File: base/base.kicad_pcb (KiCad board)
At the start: 2 copper layers, 100 x 100 mm, 32 parts, among them J1 FTDI, J2 Barrel_Jack, J3 CONN_01X40, SW1 RESET, SW2 POWER, U1 Z80CPU, U2 27C256, U3 7404, U4 55257, U5 7432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

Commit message: Added power indicator light and changed FTDI footprint
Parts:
- added D2: LED, LEDs:LED_D3.0mm, F.Cu at (105.4, 154.9)
- added R4: 470, Resistors_THT:R_Axial_DIN0207_L6.3mm_D2.5mm_P7.62mm_Horizontal, F.Cu at (115.6, 154.9)
- J1: footprint Pin_Headers:Pin_Header_Straight_1x06_Pitch2.54mm -> Pin_Headers:Pin_Header_Angled_1x06_Pitch2.54mm
- moved J1 7.62 mm to (133.3, 71.9)
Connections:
- J1 pad 2: CTS -> (no net)
- J1 pad 3: Net-(J1-Pad3) -> (no net)
- J1 pad 6: RTS -> (no net)
- SW2 pad 1: Net-(SW2-Pad1) -> (no net)
- SW2 pad 2: Net-(SW2-Pad2) -> (no net)
- U2 pad 1: Net-(U2-Pad1) -> (no net)
- U5 pad 10: Net-(U5-Pad10) -> (no net)
- U5 pad 8: Net-(U5-Pad8) -> (no net)
- U5 pad 9: Net-(U5-Pad9) -> (no net)
- U6 pad 17: Net-(U6-Pad17) -> (no net)
- U6 pad 23: Net-(U6-Pad23) -> (no net)
- U6 pad 24: Net-(U6-Pad24) -> (no net)
- U6 pad 29: Net-(U6-Pad29) -> (no net)
- U6 pad 31: Net-(U6-Pad31) -> (no net)
- U6 pad 32: Net-(U6-Pad32) -> (no net)
- U6 pad 33: Net-(U6-Pad33) -> (no net)
- U6 pad 34: Net-(U6-Pad34) -> (no net)
- U6 pad 36: Net-(U6-Pad36) -> (no net)
- U6 pad 37: Net-(U6-Pad37) -> (no net)
- U6 pad 38: Net-(U6-Pad38) -> (no net)
- U6 pad 39: Net-(U6-Pad39) -> (no net)
- X1 pad 1: Net-(X1-Pad1) -> (no net)
- X2 pad 1: Net-(X2-Pad1) -> (no net)
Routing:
- net RX: track 57.0 -> 49.3 mm
- net +5V: track 394.2 -> 400.7 mm
- net TX: track 65.7 -> 59.4 mm
- net Net-(D2-Pad1): track 0.00 -> 2.54 mm
- net (no net): track 0.00 -> 1.27 mm
- net Net-(J1-Pad3): track 0.79 -> 0.00 mm
- net Net-(U5-Pad8): track 0.63 -> 0.00 mm
- net Net-(U5-Pad10): track 0.63 -> 0.00 mm
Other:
- board text added: "CTS"
- board text added: "RTS"
- board text added: "RX<"
- board text added: "TX>"
- board text added: "Vcc"

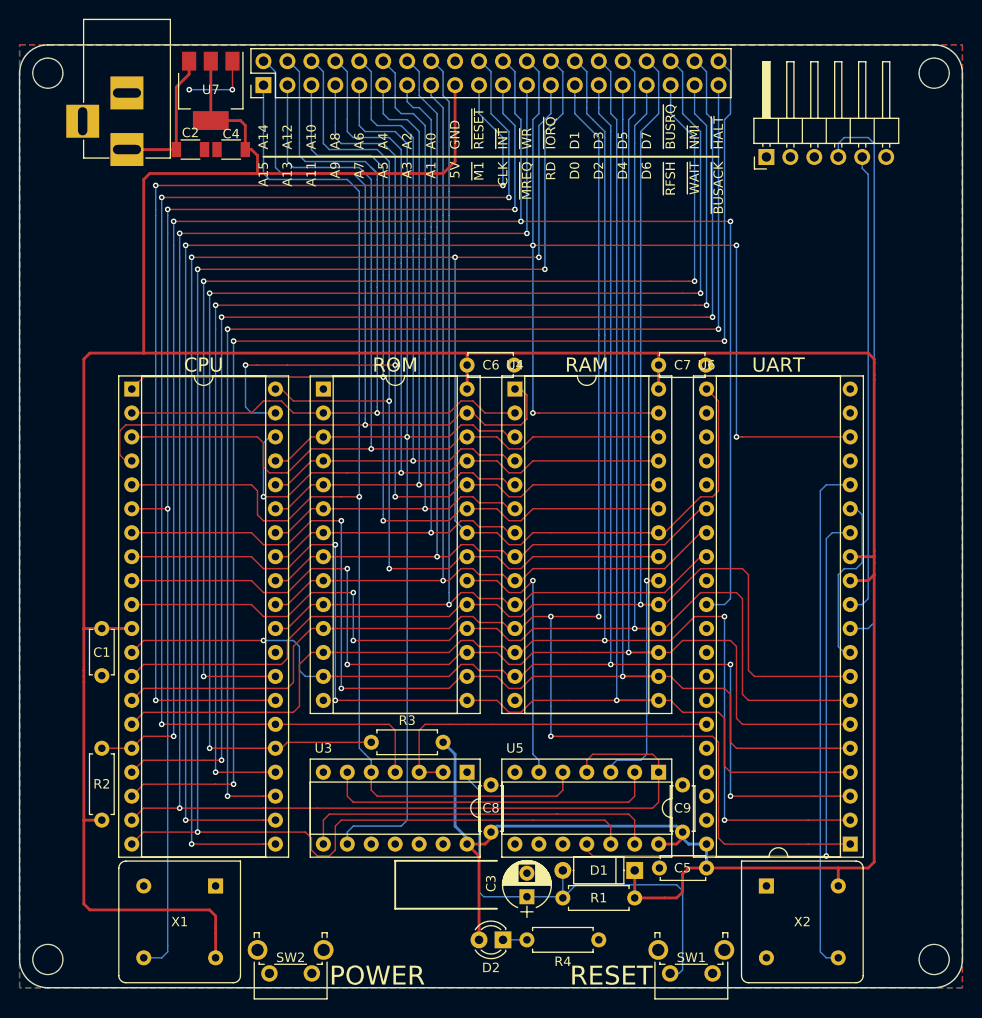
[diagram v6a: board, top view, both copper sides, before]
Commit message: Added soft power button
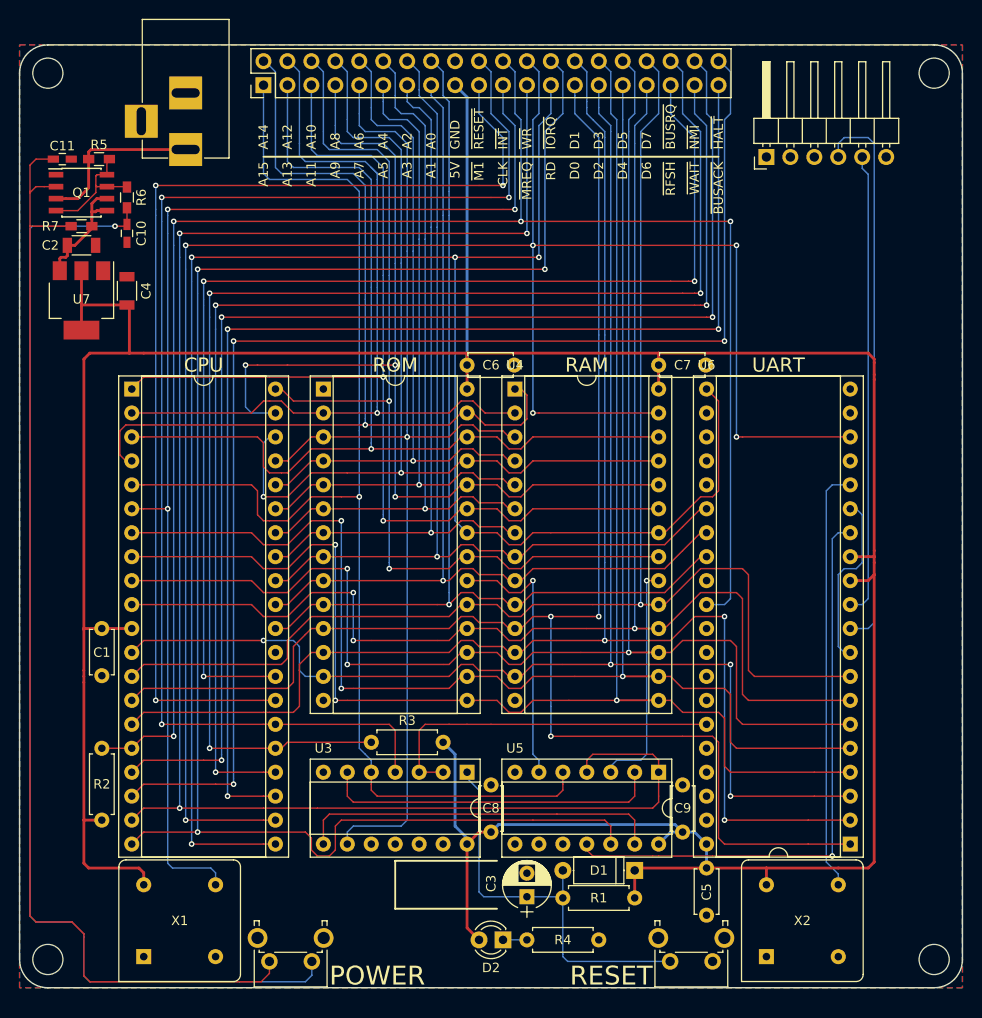
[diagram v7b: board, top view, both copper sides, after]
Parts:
- added C10: 1 uF, Capacitors_SMD:C_0603_HandSoldering, F.Cu at (65.5, 80.0)
- added C11: .1 uF, Capacitors_SMD:C_0603_HandSoldering, F.Cu at (58.7, 72.1)
- added Q1: IRF7309IPBF, Housings_SOIC:SOIC-8_3.9x4.9mm_Pitch1.27mm, F.Cu at (60.7, 75.7)
- added R5: 10k, Resistors_SMD:R_0603_HandSoldering, F.Cu at (62.6, 72.1)
- added R6: 100k, Resistors_SMD:R_0603_HandSoldering, F.Cu at (65.5, 76.2)
- added R7: 10k, Resistors_SMD:R_0603_HandSoldering, F.Cu at (60.7, 79.2)
- R4: value 470 -> 1k
- moved U7 26.1 mm to (60.7, 87.1)
- moved C4 18.6 mm to (65.5, 86.1), turned to 90 degrees
- moved C2 15.4 mm to (60.7, 81.3)
- moved X1 10.7 mm to (67.3, 156.7), turned to 0 degrees
- moved X2 7.49 mm to (133.3, 156.7), turned to 0 degrees
- moved J2 6.22 mm to (71.8, 71.1)
- moved SW1 1.27 mm to (127.6, 157.2)
- moved SW2 1.27 mm to (85.1, 157.2)
- turned C5 to 270 degrees
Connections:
- C2 pad 1: Net-(C2-Pad1) -> +VSW
- J2 pad 1: Net-(C2-Pad1) -> +VDC
- SW2 pad 1: (no net) -> Net-(C10-Pad1)
- SW2 pad 2: (no net) -> Net-(C11-Pad1)
- U7 pad 3: Net-(C2-Pad1) -> +VSW
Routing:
- net Net-(C11-Pad1): track 0.00 -> 122.3 mm
- net Net-(C10-Pad1): track 0.00 -> 122.3 mm, vias 0 -> 1
- net +5V: track 400.7 -> 352.2 mm
- net +VDC: track 0.00 -> 18.1 mm
- net Net-(C2-Pad1): track 15.5 -> 0.00 mm
- net Net-(Q1-Pad4): track 0.00 -> 13.1 mm
- net +VSW: track 0.00 -> 12.8 mm
- net Net-(U6-Pad16): track 54.5 -> 45.1 mm
- net GND: track 8.24 -> 0.00 mm, vias 2 -> 0
- net Net-(C3-Pad1): track 48.9 -> 43.3 mm
- net CLOCK: track 135.9 -> 130.5 mm
- net (no net): track 1.27 -> 0.00 mm
